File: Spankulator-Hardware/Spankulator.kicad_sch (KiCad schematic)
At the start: 99 parts, among them J1 3.5mm Jack, J12 Arduino Socket, J13 Arduino Socket, J2 2x5 Header, J3 3.5mm Jack, J4 3.5mm Jack, J5 3.5mm Jack, J6 3.5mm Jack, J7 2x5 Header, J9 Display Header, Q1 2N3904, SW1 Adj, SW2 Push Button, SW3 Push Button, SW4 Push Button, SW5 Push Button, SW6 Push Button, SW7 Push Button, SW8 Push Button, U1 TL072CP, U2 CD4013BE, U3 TL072CP, U4 MC78L05_TO92, U5 LP2950-3.3_TO92, U6 MAX7480, U7 MB85RC256, U8 MCP6002-E/P

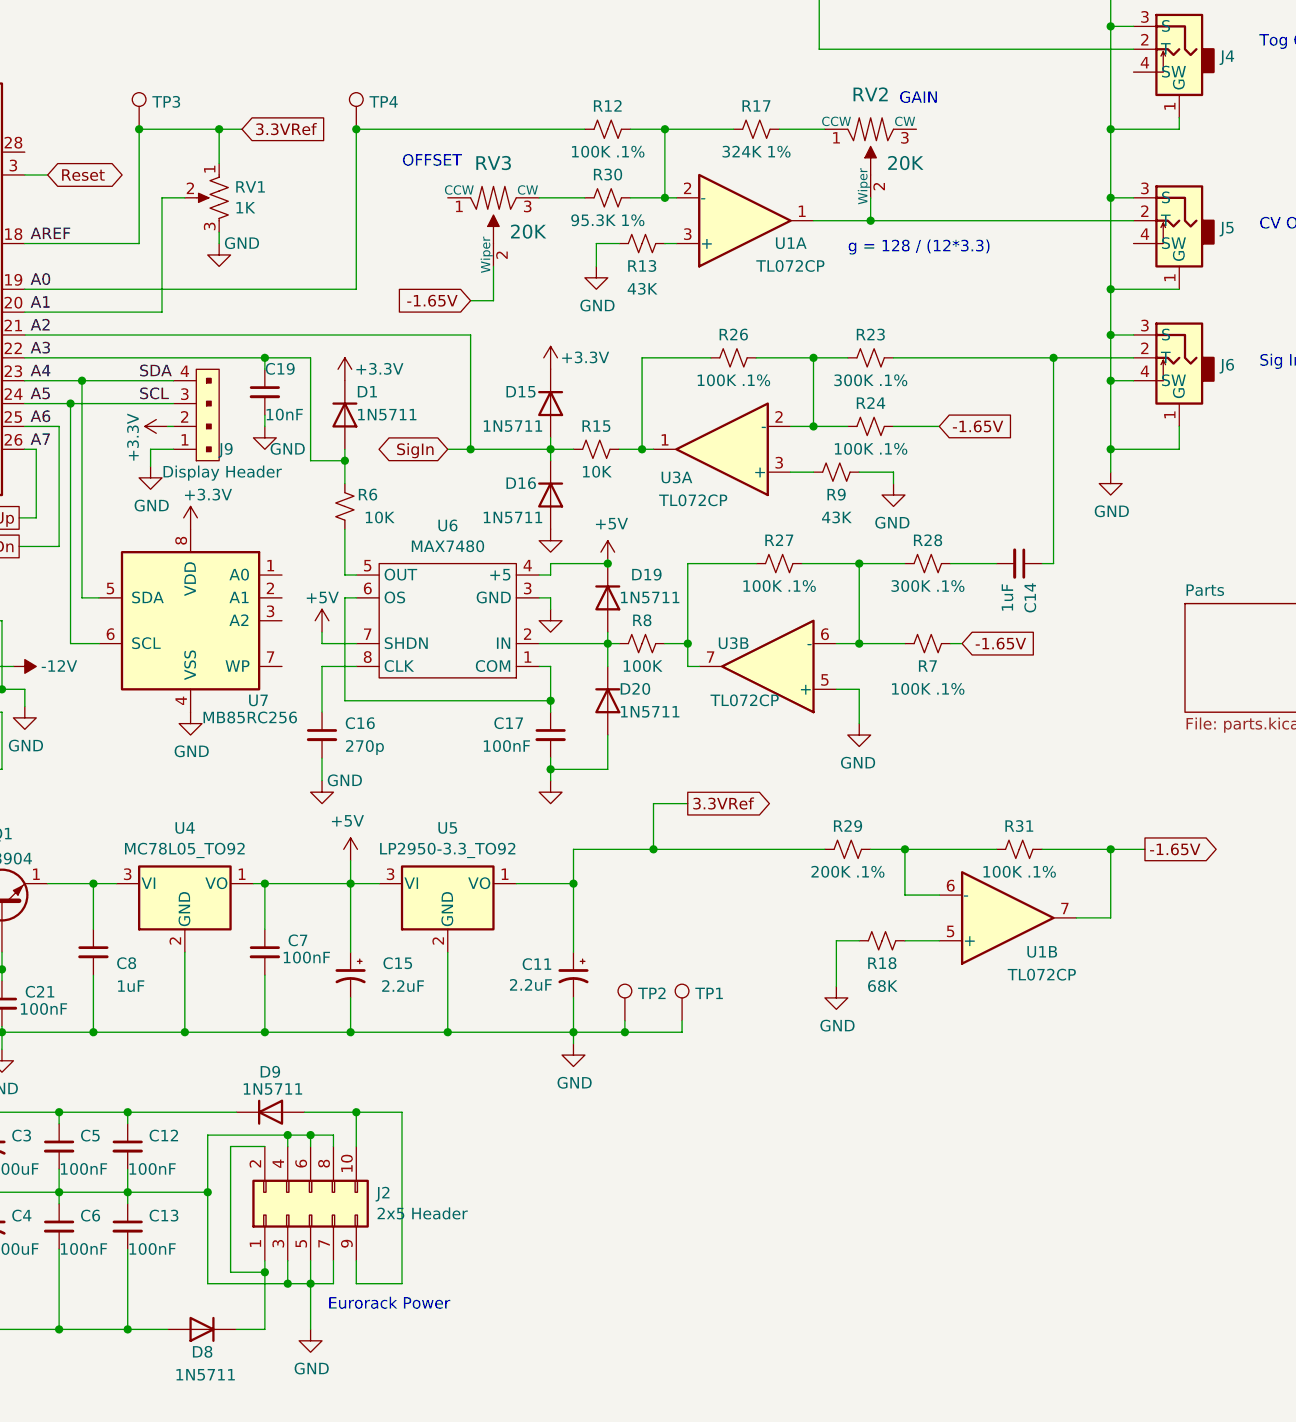
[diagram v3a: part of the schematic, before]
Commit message: Version 5.3 of the board
Updated reverse protection diode
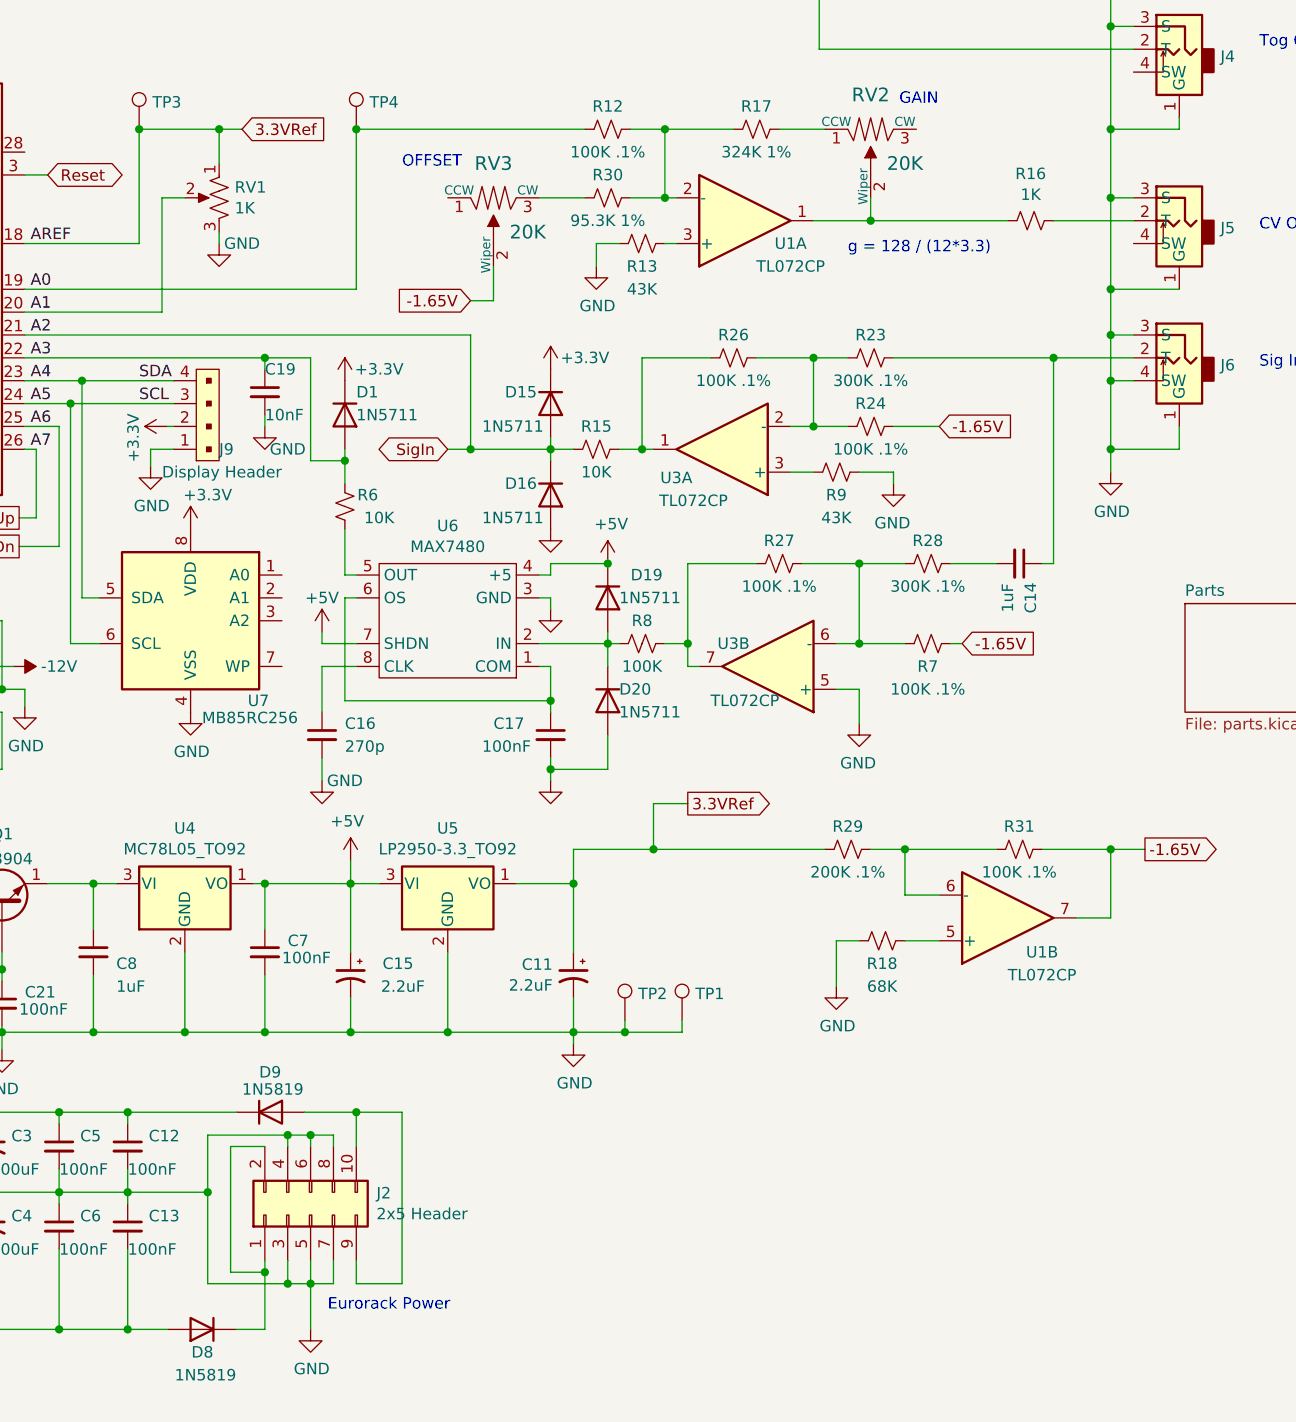
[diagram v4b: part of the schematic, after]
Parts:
- added R16: 1K, Resistor_THT:R_Axial_DIN0207_L6.3mm_D2.5mm_P10.16mm_Horizontal, symbol Device:R_Small_US
- D8: value 1N5711 -> 1N5819; footprint Diode_THT:D_DO-35_SOD27_P7.62mm_Horizontal -> Diode_THT:D_DO-41_SOD81_P2.54mm_Vertical_AnodeUp; LCSC Part # C283247 -> C110032
- D9: value 1N5711 -> 1N5819; footprint Diode_THT:D_DO-35_SOD27_P2.54mm_Vertical_KathodeUp -> Diode_THT:D_DO-41_SOD81_P2.54mm_Vertical_KathodeUp; LCSC Part # C283247 -> C110032
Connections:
- net at RV2.2 (Wiper), U1.1: now also R16.2; no longer J5.2 (T)
- new net: J5.2 (T), R16.1
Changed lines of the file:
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@@
   (title_block
     (title "Spankulator")
-    (rev "5.2")
+    (rev "5.3")
     (company "Greenface Labs")
   )
@@
     (stroke (width 0) (type default) (color 0 0 0 0))
   )
-  (wire (pts (xy 220.98 66.04) (xy 250.19 66.04))
+  (wire (pts (xy 220.98 66.04) (xy 236.22 66.04))
     (stroke (width 0) (type default) (color 0 0 0 0))
   )
@@
     (stroke (width 0) (type default) (color 0 0 0 0))
   )
+  (wire (pts (xy 241.3 66.04) (xy 250.19 66.04))
+    (stroke (width 0) (type default) (color 0 0 0 0))
+  )
   (wire (pts (xy 147.32 173.99) (xy 147.32 184.15))
     (stroke (width 0) (type default) (color 0 0 0 0))
@@
     (pin "2")
   )
+  (symbol (lib_id "Device:R_Small_US") (at 238.76 66.04 270) (unit 1)
+    (in_bom yes) (on_board yes)
+    (property "Reference" "R16" (id 0) (at 238.76 60.833 90))
+    (property "Value" "1K" (id 1) (at 238.76 63.1444 90))
+    (property "Footprint" "Resistor_THT:R_Axial_DIN0207_L6.3mm_D2.5mm_P10.16mm_Horizontal" (id 2) (at 238.76 66.04 0)
+      (effects (font (size 1.27 1.27)) hide)
+    )
+    (property "Datasheet" "~" (id 3) (at 238.76 66.04 0)
+      (effects (font (size 1.27 1.27)) hide)
+    )
+    (property "Digi-Key Part" "CF14JT1K00CT-ND" (id 4) (at 238.76 66.04 90)
+      (effects (font (size 1.27 1.27)) hide)
+    )
+    (property "LCSC Part #" "C66649" (id 5) (at 238.76 66.04 0)
+      (effects (font (size 1.27 1.27)) hide)
+    )
+    (pin "1")
+    (pin "2")
+  )
   (symbol (lib_id "Diode:1N4148") (at 154.305 165.1 0) (unit 1)
     (in_bom yes) (on_board yes)
@@
       (effects (font (size 1.27 1.27)) (justify left))
     )
-    (property "Value" "1N5711" (id 1) (at 151.13 162.56 0)
+    (property "Value" "1N5819" (id 1) (at 151.13 162.56 0)
       (effects (font (size 1.27 1.27)) (justify left))
     )
-    (property "Footprint" "Diode_THT:D_DO-35_SOD27_P2.54mm_Vertical_KathodeUp" (id 2) (at 154.305 169.545 0)
+    (property "Footprint" "Diode_THT:D_DO-41_SOD81_P2.54mm_Vertical_KathodeUp" (id 2) (at 154.305 169.545 0)
       (effects (font (size 1.27 1.27)) hide)
     )
@@
       (effects (font (size 1.27 1.27)) hide)
     )
-    (property "LCSC Part #" "C283247" (id 5) (at 154.305 165.1 0)
+    (property "LCSC Part #" "C110032" (id 5) (at 154.305 165.1 0)
       (effects (font (size 1.27 1.27)) hide)
     )
@@
       (effects (font (size 1.27 1.27)) (justify left))
     )
-    (property "Value" "1N5711" (id 1) (at 150.495 194.31 0)
+    (property "Value" "1N5819" (id 1) (at 150.495 194.31 0)
       (effects (font (size 1.27 1.27)) (justify left))
     )
-    (property "Footprint" "Diode_THT:D_DO-35_SOD27_P7.62mm_Horizontal" (id 2) (at 146.685 184.785 0)
+    (property "Footprint" "Diode_THT:D_DO-41_SOD81_P2.54mm_Vertical_AnodeUp" (id 2) (at 146.685 184.785 0)
       (effects (font (size 1.27 1.27)) hide)
     )
@@
       (effects (font (size 1.27 1.27)) hide)
     )
-    (property "LCSC Part #" "C283247" (id 5) (at 146.685 189.23 0)
+    (property "LCSC Part #" "C110032" (id 5) (at 146.685 189.23 0)
       (effects (font (size 1.27 1.27)) hide)
     )
@@
     )
     (path "/ffb6f1cc-502c-44ab-af5c-1e16fc95c761"
-      (reference "D8") (unit 1) (value "1N5711") (footprint "Diode_THT:D_DO-35_SOD27_P7.62mm_Horizontal")
+      (reference "D8") (unit 1) (value "1N5819") (footprint "Diode_THT:D_DO-41_SOD81_P2.54mm_Vertical_AnodeUp")
     )
     (path "/e4a3c8d3-a1ce-43f4-982e-7455d6f0fe81"
-      (reference "D9") (unit 1) (value "1N5711") (footprint "Diode_THT:D_DO-35_SOD27_P2.54mm_Vertical_KathodeUp")
+      (reference "D9") (unit 1) (value "1N5819") (footprint "Diode_THT:D_DO-41_SOD81_P2.54mm_Vertical_KathodeUp")
     )
     (path "/00000000-0000-0000-0000-00005ec79b09"
@@
       (reference "R15") (unit 1) (value "10K") (footprint "Resistor_THT:R_Axial_DIN0207_L6.3mm_D2.5mm_P10.16mm_Horizontal")
     )
+    (path "/e07530a7-8a01-4924-9200-735d32c1129f"
+      (reference "R16") (unit 1) (value "1K") (footprint "Resistor_THT:R_Axial_DIN0207_L6.3mm_D2.5mm_P10.16mm_Horizontal")
+    )
     (path "/00000000-0000-0000-0000-00005f427c66"
